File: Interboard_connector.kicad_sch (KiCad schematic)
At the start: 2 parts, among them J1 Chainbus in, J2 Chainbus Out

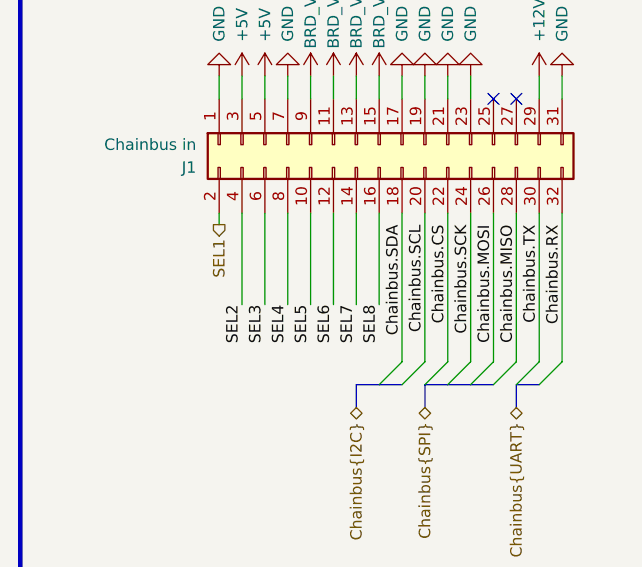
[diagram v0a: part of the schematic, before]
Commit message: ServoController
Dodano arkusz sterownika servo, aktualizacja polaczen
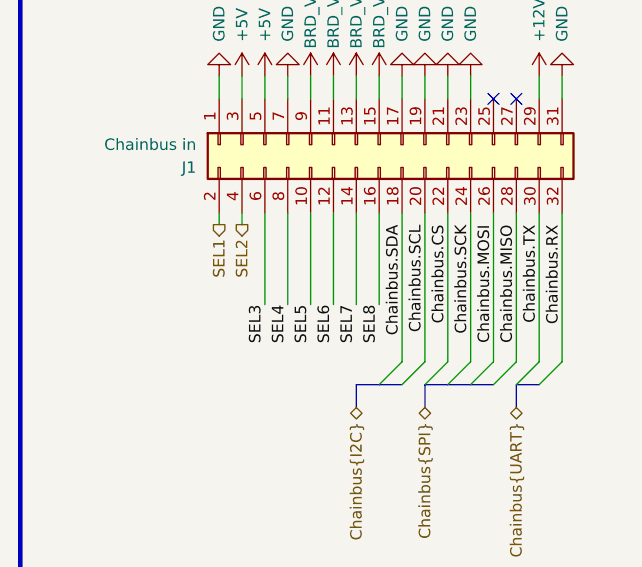
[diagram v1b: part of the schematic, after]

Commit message: PCB design
In progress
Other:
- title: MMS3 Hat template small (Change Me) -> MMS3 Hat servo controller
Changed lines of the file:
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@@
 	(paper "A4")
 	(title_block
-		(title "MMS3 Hat template small (Change Me)")
+		(title "MMS3 Hat servo controller")
 		(date "2026-02-25")
 		(rev "A")
